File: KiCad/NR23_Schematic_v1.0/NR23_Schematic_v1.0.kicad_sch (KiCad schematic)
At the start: 0 parts

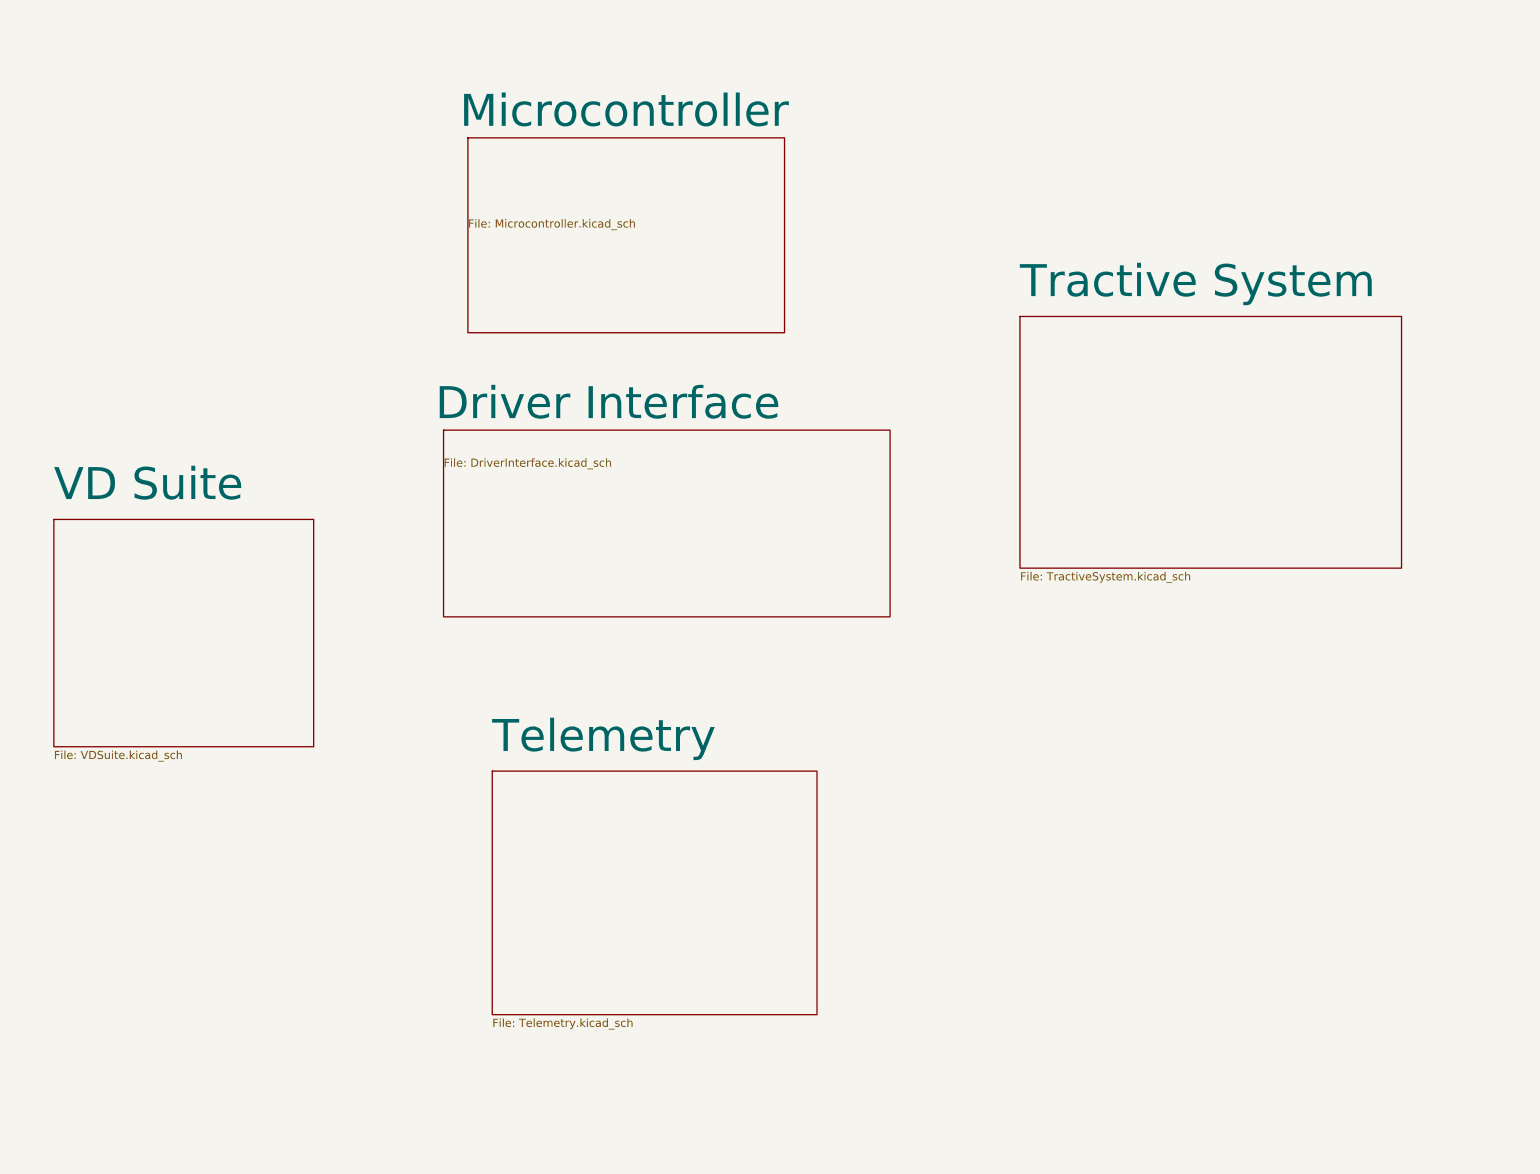
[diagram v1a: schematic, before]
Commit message: added benchtop model schematic
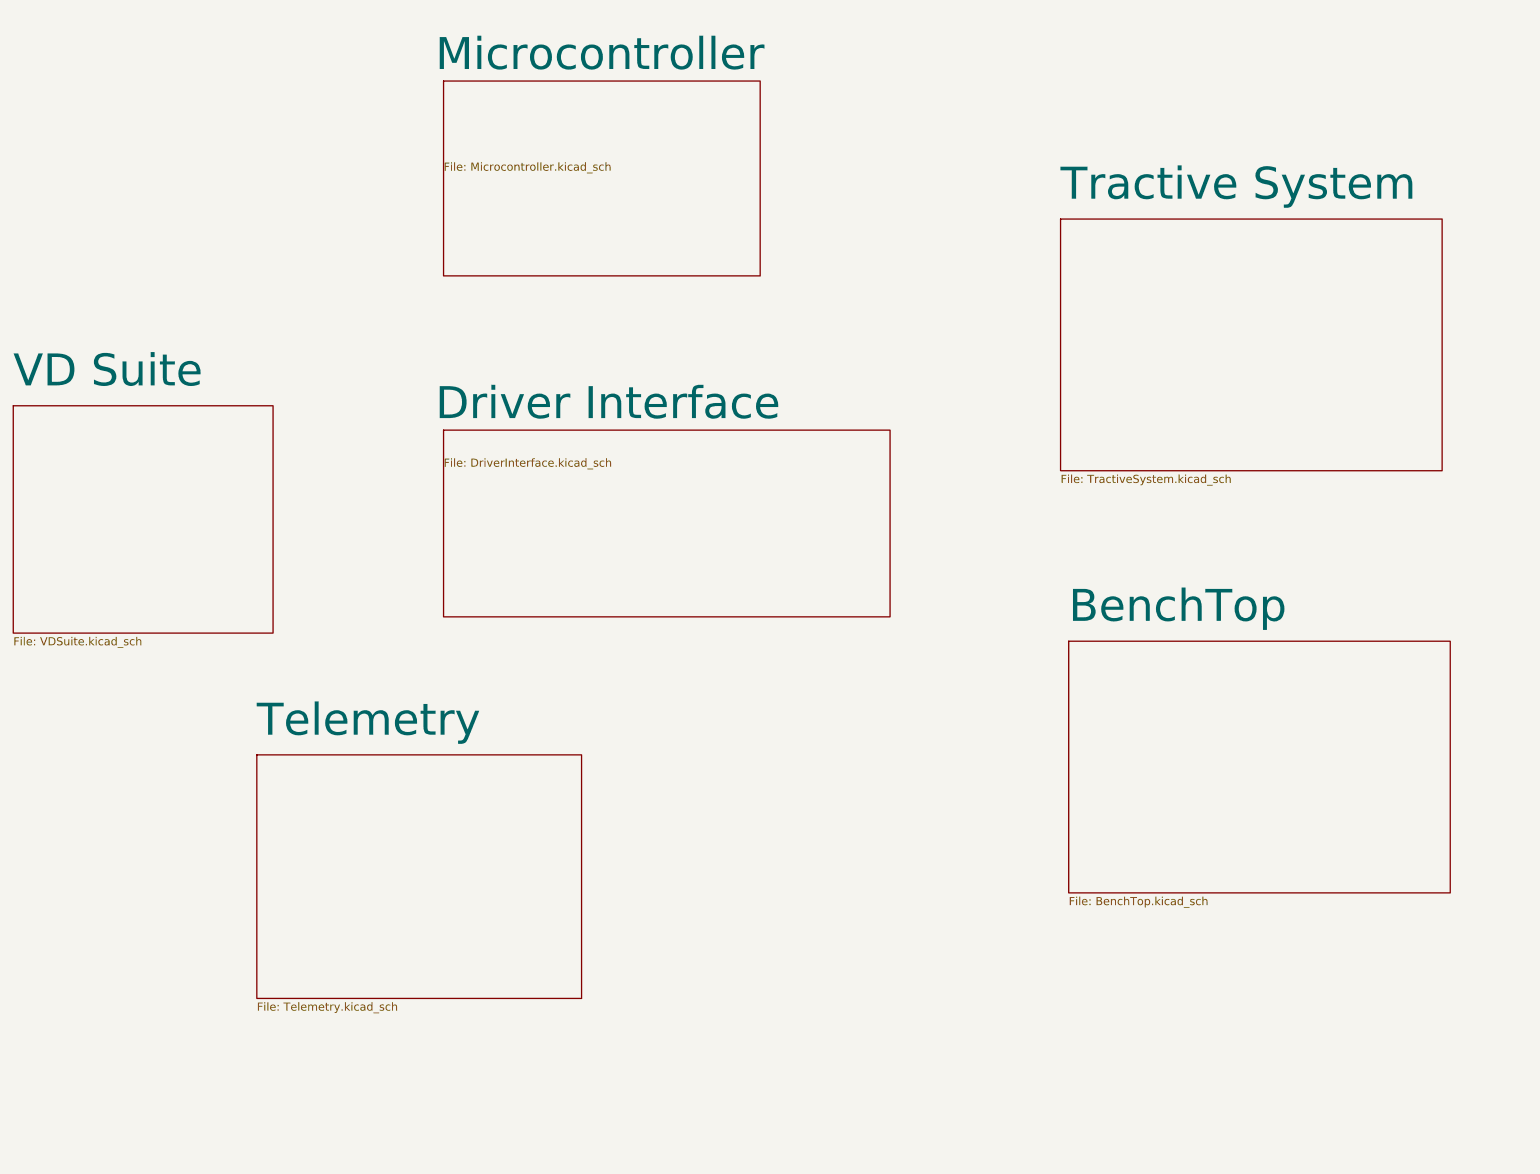
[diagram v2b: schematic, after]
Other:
- added sheet BenchTop (BenchTop.kicad_sch)
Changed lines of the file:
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@@
   (paper "A")
   (title_block
-    (date "2023-02-28")
+    (date "2023-03-03")
   )
-  (sheet (at 96.52 135.89) (size 50.8 38.1)
+  (sheet (at 59.69 133.35) (size 50.8 38.1)
     (stroke (width 0.1524) (type solid) (color 0 0 0 0))
     (fill (color 0 0 0 0.0000))
-    (property "Sheet name" "Telemetry" (id 0) (at 96.52 133.35 0)
+    (property "Sheet name" "Telemetry" (id 0) (at 59.69 130.81 0)
       (effects (font (size 5 5)) (justify left bottom))
     )
-    (property "Sheet file" "Telemetry.kicad_sch" (id 1) (at 96.52 174.5746 0)
+    (property "Sheet file" "Telemetry.kicad_sch" (id 1) (at 59.69 172.0346 0)
       (effects (font (size 1.27 1.27)) (justify left top))
     )
   )
-  (sheet (at 27.94 96.52) (size 40.64 35.56) (fields_autoplaced)
+  (sheet (at 21.59 78.74) (size 40.64 35.56) (fields_autoplaced)
     (stroke (width 0.1524) (type solid) (color 0 0 0 0))
     (fill (color 0 0 0 0.0000))
-    (property "Sheet name" "VD Suite" (id 0) (at 27.94 93.9434 0)
+    (property "Sheet name" "VD Suite" (id 0) (at 21.59 76.1634 0)
       (effects (font (size 5 5)) (justify left bottom))
     )
-    (property "Sheet file" "VDSuite.kicad_sch" (id 1) (at 27.94 132.6646 0)
+    (property "Sheet file" "VDSuite.kicad_sch" (id 1) (at 21.59 114.8846 0)
       (effects (font (size 1.27 1.27)) (justify left top))
     )
@@
     )
   )
-  (sheet (at 179.07 64.77) (size 59.69 39.37) (fields_autoplaced)
+  (sheet (at 186.69 115.57) (size 59.69 39.37) (fields_autoplaced)
     (stroke (width 0.1524) (type solid) (color 0 0 0 0))
     (fill (color 0 0 0 0.0000))
-    (property "Sheet name" "Tractive System" (id 0) (at 179.07 62.1934 0)
+    (property "Sheet name" "BenchTop" (id 0) (at 186.69 112.9934 0)
       (effects (font (size 5 5)) (justify left bottom))
     )
-    (property "Sheet file" "TractiveSystem.kicad_sch" (id 1) (at 179.07 104.7246 0)
+    (property "Sheet file" "BenchTop.kicad_sch" (id 1) (at 186.69 155.5246 0)
       (effects (font (size 1.27 1.27)) (justify left top))
     )
   )
-  (sheet (at 92.71 36.83) (size 49.53 30.48)
+  (sheet (at 185.42 49.53) (size 59.69 39.37) (fields_autoplaced)
     (stroke (width 0.1524) (type solid) (color 0 0 0 0))
     (fill (color 0 0 0 0.0000))
-    (property "Sheet name" "Microcontroller" (id 0) (at 91.44 35.56 0)
+    (property "Sheet name" "Tractive System" (id 0) (at 185.42 46.9534 0)
       (effects (font (size 5 5)) (justify left bottom))
     )
-    (property "Sheet file" "Microcontroller.kicad_sch" (id 1) (at 92.71 49.53 0)
+    (property "Sheet file" "TractiveSystem.kicad_sch" (id 1) (at 185.42 89.4846 0)
+      (effects (font (size 1.27 1.27)) (justify left top))
+    )
+  )
+  (sheet (at 88.9 27.94) (size 49.53 30.48)
+    (stroke (width 0.1524) (type solid) (color 0 0 0 0))
+    (fill (color 0 0 0 0.0000))
+    (property "Sheet name" "Microcontroller" (id 0) (at 87.63 26.67 0)
+      (effects (font (size 5 5)) (justify left bottom))
+    )
+    (property "Sheet file" "Microcontroller.kicad_sch" (id 1) (at 88.9 40.64 0)
       (effects (font (size 1.27 1.27)) (justify left top))
     )
@@
     (path "/16ced548-a4c4-4a05-b722-8e9610f878cc" (page "5"))
     (path "/8302703f-65d0-4b91-aeea-6f721ab57e4c" (page "6"))
+    (path "/6b38ef1b-89ba-46d1-8032-b895c26a5218" (page "7"))
   )
   (symbol_instances
@@
       (reference "BT?") (unit 1) (value "12V") (footprint "")
     )
+    (path "/6b38ef1b-89ba-46d1-8032-b895c26a5218/9ec1d7fc-6f5f-41a1-a450-d625e8c70d57"
+      (reference "BT?") (unit 1) (value "12V") (footprint "")
+    )
+    (path "/6b38ef1b-89ba-46d1-8032-b895c26a5218/a05e3eb6-24ad-4681-b9d3-ba583a4db1b6"
+      (reference "BT?") (unit 1) (value "7.2KW_Battery") (footprint "")
+    )
     (path "/8302703f-65d0-4b91-aeea-6f721ab57e4c/a05e3eb6-24ad-4681-b9d3-ba583a4db1b6"
       (reference "BT?") (unit 1) (value "7.2KW_Battery") (footprint "")
@@
       (reference "F?") (unit 1) (value "Fuse") (footprint "")
     )
+    (path "/6b38ef1b-89ba-46d1-8032-b895c26a5218/ba497376-f3b3-4aa7-8c24-837b232c4c3d"
+      (reference "F?") (unit 1) (value "Fuse") (footprint "")
+    )
     (path "/8302703f-65d0-4b91-aeea-6f721ab57e4c/f89e7d82-128e-4a2c-9534-2de10c90326b"
       (reference "F?") (unit 1) (value "Fuse") (footprint "")
     )
+    (path "/6b38ef1b-89ba-46d1-8032-b895c26a5218/f89e7d82-128e-4a2c-9534-2de10c90326b"
+      (reference "F?") (unit 1) (value "Fuse") (footprint "")
+    )
     (path "/8302703f-65d0-4b91-aeea-6f721ab57e4c/dc0c9514-aba3-4b23-943d-072d1b6ac9ac"
-      (reference "J?") (unit 1) (value "Conn_01x06_Female") (footprint "")
+      (reference "J?") (unit 1) (value "F_con") (footprint "")
+    )
+    (path "/6b38ef1b-89ba-46d1-8032-b895c26a5218/dc0c9514-aba3-4b23-943d-072d1b6ac9ac"
+      (reference "J?") (unit 1) (value "F_con") (footprint "")
     )
     (path "/8302703f-65d0-4b91-aeea-6f721ab57e4c/de29f7ed-664a-479e-9fdb-f102e88408fb"
-      (reference "J?") (unit 1) (value "Conn_01x06_Male") (footprint "")
+      (reference "J?") (unit 1) (value "M_con") (footprint "")
+    )
+    (path "/6b38ef1b-89ba-46d1-8032-b895c26a5218/de29f7ed-664a-479e-9fdb-f102e88408fb"
+      (reference "J?") (unit 1) (value "M_con") (footprint "")
     )
     (path "/8302703f-65d0-4b91-aeea-6f721ab57e4c/91be2d7e-1603-4ffc-85db-9cef433a5348"
       (reference "K?") (unit 1) (value "Key Switch Relay") (footprint "Relay_THT:Relay_1P1T_NO_10x24x18.8mm_Panasonic_ADW11xxxxW_THT")
     )
+    (path "/6b38ef1b-89ba-46d1-8032-b895c26a5218/91be2d7e-1603-4ffc-85db-9cef433a5348"
+      (reference "K?") (unit 1) (value "Key Switch Relay") (footprint "Relay_THT:Relay_1P1T_NO_10x24x18.8mm_Panasonic_ADW11xxxxW_THT")
+    )
     (path "/8302703f-65d0-4b91-aeea-6f721ab57e4c/b190c8cb-bd8a-4856-a017-7c47d784415d"
       (reference "K?") (unit 1) (value "Line Contactor") (footprint "Relay_THT:Relay_1P1T_NO_10x24x18.8mm_Panasonic_ADW11xxxxW_THT")
+    )
+    (path "/6b38ef1b-89ba-46d1-8032-b895c26a5218/b190c8cb-bd8a-4856-a017-7c47d784415d"
+      (reference "K?") (unit 1) (value "Line Contactor") (footprint "Relay_THT:Relay_1P1T_NO_10x24x18.8mm_Panasonic_ADW11xxxxW_THT")
+    )
+    (path "/6b38ef1b-89ba-46d1-8032-b895c26a5218/17f5dc4f-ba2e-4459-9469-5c2da575d700"
+      (reference "M1") (unit 1) (value "Zero_7R_Motor") (footprint "")
     )
     (path "/8302703f-65d0-4b91-aeea-6f721ab57e4c/17f5dc4f-ba2e-4459-9469-5c2da575d700"
@@
       (reference "SW?") (unit 1) (value "Key Switch") (footprint "")
     )
+    (path "/6b38ef1b-89ba-46d1-8032-b895c26a5218/737b7baf-b889-4aeb-8cad-49a9c6801593"
+      (reference "SW?") (unit 1) (value "Key Switch") (footprint "")
+    )
     (path "/8302703f-65d0-4b91-aeea-6f721ab57e4c/839a2160-4be7-4a71-b4f3-e2d027441525"
+      (reference "SW?") (unit 1) (value "HV Safety Switch") (footprint "")
+    )
+    (path "/6b38ef1b-89ba-46d1-8032-b895c26a5218/839a2160-4be7-4a71-b4f3-e2d027441525"
       (reference "SW?") (unit 1) (value "HV Safety Switch") (footprint "")
     )
@@
       (reference "U?") (unit 1) (value "Throttle") (footprint "")
     )
+    (path "/6b38ef1b-89ba-46d1-8032-b895c26a5218/0aa54167-f3d9-467b-bc69-db1827651c6c"
+      (reference "U?") (unit 1) (value "Throttle") (footprint "")
+    )
+    (path "/6b38ef1b-89ba-46d1-8032-b895c26a5218/35333229-0e5e-47a2-bb43-fcfbf8fd658d"
+      (reference "U?") (unit 1) (value "Sevcon_Gen4_Size6") (footprint "")
+    )
     (path "/8302703f-65d0-4b91-aeea-6f721ab57e4c/35333229-0e5e-47a2-bb43-fcfbf8fd658d"
